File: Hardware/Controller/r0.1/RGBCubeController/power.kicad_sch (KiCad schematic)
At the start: 43 parts, among them J6 Battery, Q1 AON7804, U6 LTC4365TS8, U7 AP64350, U8 AP64350

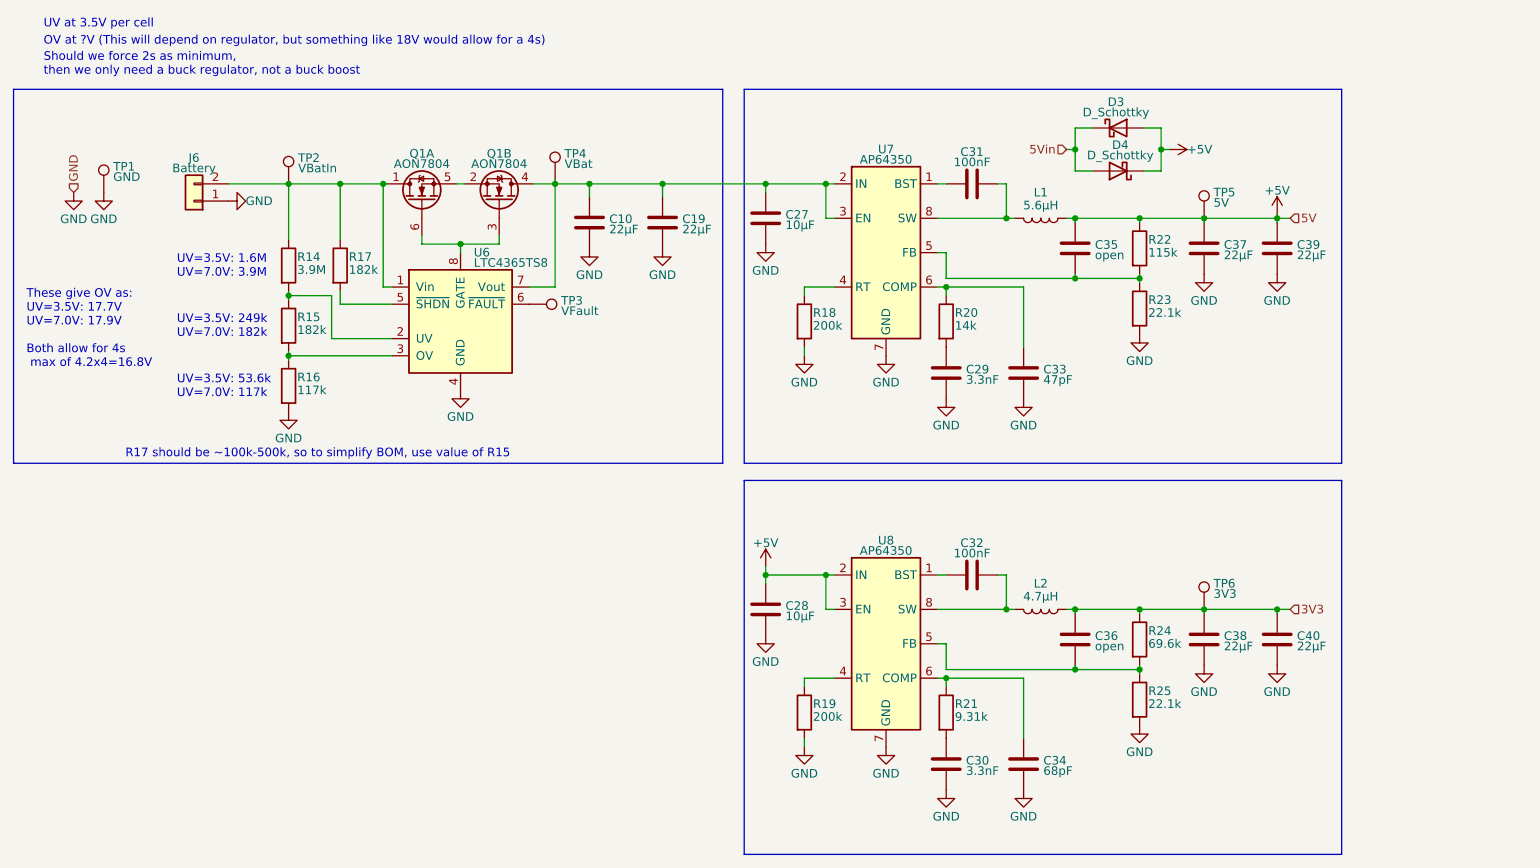
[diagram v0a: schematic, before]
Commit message: [RGBCubeController] Switched to using the Unexpected Maker TinyS3 ESP32 S3 dev board. This removes the need for a 3V3 regulator, reduces the number of components, as well as improving the main microcontroller. It is more expensive, and also takes up more space. Currently parts are all placed on the board (except for the power switch), but no routing has been done.
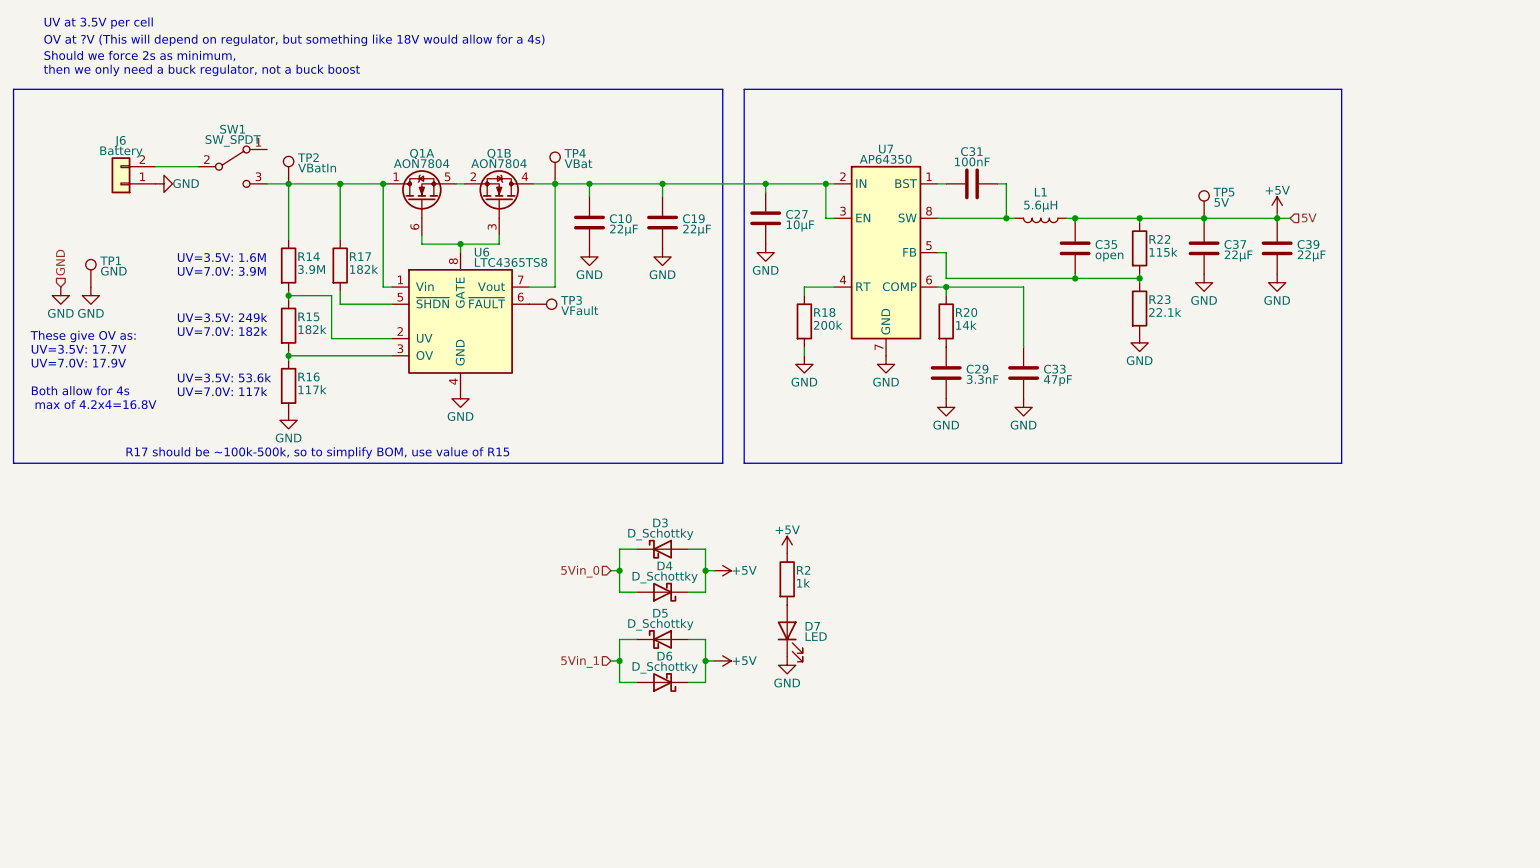
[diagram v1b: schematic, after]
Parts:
- removed C28: 10μF, Capacitor_SMD:C_0603_1608Metric, symbol Device:C
- removed C30: 3.3nF, Capacitor_SMD:C_0603_1608Metric, symbol Device:C
- removed C32: 100nF, Capacitor_SMD:C_0603_1608Metric, symbol Device:C
- removed C34: 68pF, Capacitor_SMD:C_0603_1608Metric, symbol Device:C
- removed C36: open, Capacitor_SMD:C_0603_1608Metric, symbol Device:C
- removed C38, C40: 22μF, Capacitor_SMD:C_0603_1608Metric, symbol Device:C
- removed L2: 4.7μH, Inductor_SMD:L_Wuerth_MAPI-3015, symbol Device:L
- removed R19: 200k, Resistor_SMD:R_0603_1608Metric, symbol Device:R
- removed R21: 9.31k, Resistor_SMD:R_0603_1608Metric, symbol Device:R
- removed R24: 69.6k, Resistor_SMD:R_0603_1608Metric, symbol Device:R
- removed R25: 22.1k, Resistor_SMD:R_0603_1608Metric, symbol Device:R
- removed TP6: 3V3, TestPoint:TestPoint_Pad_D1.0mm, symbol Connector:TestPoint
- removed U8: AP64350, Package_SO:Diodes_SO-8EP, symbol AP64350:AP64350
- added D5, D6: D_Schottky, Diode_SMD:D_SOD-123F, symbol Device:D_Schottky
- added D7: LED, LED_SMD:LED_0603_1608Metric, symbol Device:LED
- added R2: 1k, Resistor_SMD:R_0603_1608Metric, symbol Device:R
- added SW1: SW_SPDT, symbol Switch:SW_SPDT
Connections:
- net +5V: now also D5.2 (A), D6.1 (K), R2.1
- net EP: now also D7.1 (K)
- net at Q1.1 (D), R14.1, R17.1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: now also SW1.3 (C); no longer J6.2 (Pin_2)
- net 5Vin renamed 5Vin_0
- new net: D7.2 (A), R2.2
- new net: J6.2 (Pin_2), SW1.2 (B)
- new net 5Vin_1: D5.1 (K), D6.2 (A)
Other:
- moved on the sheet: D3, D4, J6, TP1

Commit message: [RGBCubeController] Added power off switch. There will still be ~10 - 20uA current draw when off, so battery should be disconnected for long term storage. Still need to route everything.
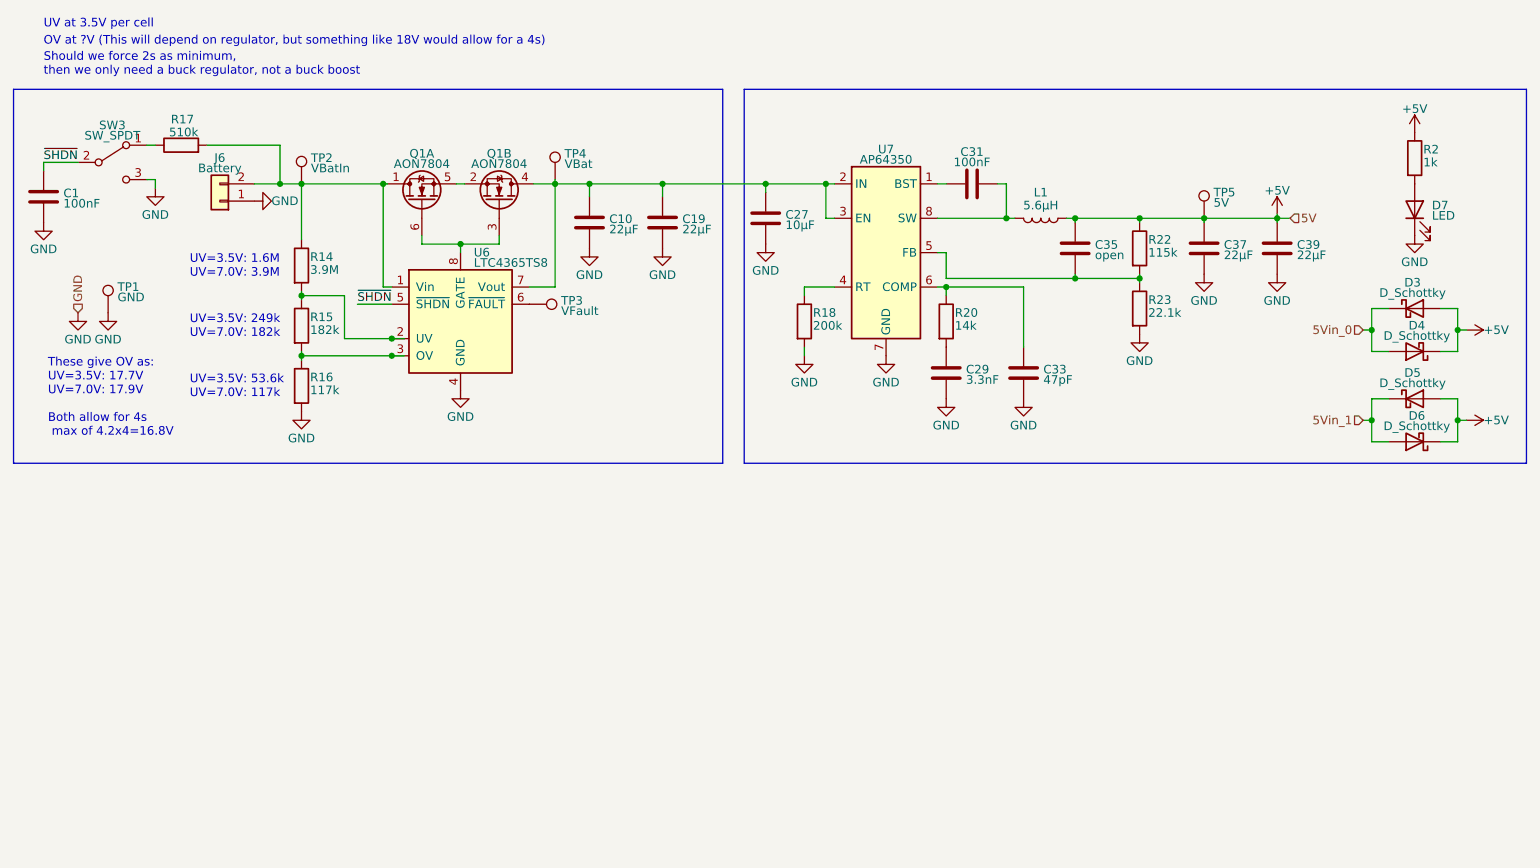
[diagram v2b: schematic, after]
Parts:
- removed SW1: SW_SPDT, symbol Switch:SW_SPDT
- added C1: 100nF, Capacitor_SMD:C_0603_1608Metric, symbol Device:C
- added SW3: SW_SPDT, Button_Switch_SMD:SW_SPDT_PCM12, symbol Switch:SW_SPDT
- R17: value 182k -> 510k
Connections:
- net EP: now also C1.1, SW3.3 (C)
- net at Q1.1 (D), R14.1, TP2.1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: now also J6.2 (Pin_2), R17.2; no longer R17.1
- net ~{SHDN}: now reaches U6.5 (~{SHDN})
- net ~{SHDN}: now also C1.2, SW3.2 (B); no longer R17.2
- new net: R17.1, SW3.1 (A)
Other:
- note removed: "R17 should be ~100k-500k, so to simplify BOM, use value of R15"
- moved on the sheet: D3, D4, D5, D6, D7, J6, R14, R15, R16, R17, R2, TP1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

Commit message: [RGBCubeController] Added Qwiic connector, as well as a pattern to the silkscreen on backside of PCB.
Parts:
- added TP6: GND, CustomTestPoint.pretty:TestPoint_Pad_D1.0mm, symbol Connector:TestPoint
- TP1, TP2, TP3, TP4, TP5: footprint TestPoint:TestPoint_Pad_D1.0mm -> CustomTestPoint.pretty:TestPoint_Pad_D1.0mm
- U6: footprint Package_TO_SOT_SMD:TSOT-23-8 -> TSOT:TSOT-23-8
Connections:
- net EP: now also TP6.1
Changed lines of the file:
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@@
-(kicad_sch (version 20220104) (generator eeschema)
+(kicad_sch (version 20220126) (generator eeschema)
   (paper "A4")
   (junction (at 184.785 45.085) (diameter 0) (color 0 0 0 0)
@@
       (effects (font (size 1.27 1.27)) (justify left))
     )
-    (property "Footprint" "TestPoint:TestPoint_Pad_D1.0mm" (id 2) (at 199.39 45.085 0)
+    (property "Footprint" "CustomTestPoint.pretty:TestPoint_Pad_D1.0mm" (id 2) (at 199.39 45.085 0)
       (effects (font (size 1.27 1.27)) hide)
     )
@@
       (effects (font (size 1.27 1.27)) (justify left))
     )
-    (property "Footprint" "TestPoint:TestPoint_Pad_D1.0mm" (id 2) (at 66.04 40.005 0)
+    (property "Footprint" "CustomTestPoint.pretty:TestPoint_Pad_D1.0mm" (id 2) (at 66.04 40.005 0)
       (effects (font (size 1.27 1.27)) hide)
     )
@@
       (effects (font (size 1.27 1.27)) (justify left))
     )
-    (property "Footprint" "TestPoint:TestPoint_Pad_D1.0mm" (id 2) (at 103.505 39.37 0)
+    (property "Footprint" "CustomTestPoint.pretty:TestPoint_Pad_D1.0mm" (id 2) (at 103.505 39.37 0)
       (effects (font (size 1.27 1.27)) hide)
     )
@@
       (effects (font (size 1.27 1.27)) (justify left))
     )
-    (property "Footprint" "TestPoint:TestPoint_Pad_D1.0mm" (id 2) (at 37.465 59.055 0)
+    (property "Footprint" "CustomTestPoint.pretty:TestPoint_Pad_D1.0mm" (id 2) (at 37.465 59.055 0)
       (effects (font (size 1.27 1.27)) hide)
     )
@@
       (effects (font (size 1.27 1.27)) (justify left))
     )
-    (property "Footprint" "Package_TO_SOT_SMD:TSOT-23-8" (id 2) (at 76.835 53.975 0)
+    (property "Footprint" "TSOT:TSOT-23-8" (id 2) (at 76.835 53.975 0)
       (effects (font (size 1.27 1.27)) hide)
     )
@@
     (pin "1")
   )
+  (symbol (lib_id "Connector:TestPoint") (at 215.9 45.085 0) (unit 1)
+    (in_bom yes) (on_board yes) (fields_autoplaced)
+    (property "Reference" "TP6" (id 0) (at 217.297 41.2623 0)
+      (effects (font (size 1.27 1.27)) (justify left))
+    )
+    (property "Value" "GND" (id 1) (at 217.297 42.7863 0)
+      (effects (font (size 1.27 1.27)) (justify left))
+    )
+    (property "Footprint" "CustomTestPoint.pretty:TestPoint_Pad_D1.0mm" (id 2) (at 220.98 45.085 0)
+      (effects (font (size 1.27 1.27)) hide)
+    )
+    (property "Datasheet" "~" (id 3) (at 220.98 45.085 0)
+      (effects (font (size 1.27 1.27)) hide)
+    )
+    (pin "1")
+  )
   (symbol (lib_id "Device:L") (at 170.18 45.085 270) (unit 1)
     (in_bom yes) (on_board yes)
@@
     (pin "2")
   )
+  (symbol (lib_id "power:GND") (at 215.9 45.085 0) (unit 1)
+    (in_bom yes) (on_board yes) (fields_autoplaced)
+    (property "Reference" "#PWR0130" (id 0) (at 215.9 51.435 0)
+      (effects (font (size 1.27 1.27)) hide)
+    )
+    (property "Value" "GND" (id 1) (at 215.9 49.022 0)
+      (effects (font (size 1.27 1.27)))
+    )
+    (property "Footprint" "" (id 2) (at 215.9 45.085 0)
+      (effects (font (size 1.27 1.27)) hide)
+    )
+    (property "Datasheet" "" (id 3) (at 215.9 45.085 0)
+      (effects (font (size 1.27 1.27)) hide)
+    )
+    (pin "1")
+  )
   (symbol (lib_id "Connector:TestPoint") (at 94.615 57.785 270) (unit 1)
     (in_bom yes) (on_board yes) (fields_autoplaced)
@@
       (effects (font (size 1.27 1.27)) (justify left))
     )
-    (property "Footprint" "TestPoint:TestPoint_Pad_D1.0mm" (id 2) (at 94.615 62.865 0)
-      (effects (font (size 1.27 1.27)) hide)
-    )
+    (property "Footprint" "CustomTestPoint.pretty:TestPoint_Pad_D1.0mm" (id 2) (at 94.615 62.865 0)
+      (effects (font (size 1.27 1.27)) hide)
+    )
